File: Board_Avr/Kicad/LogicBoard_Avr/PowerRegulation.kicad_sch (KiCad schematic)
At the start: 8 parts, among them U3 LM1117-3.3, U4 LM1117-5.0

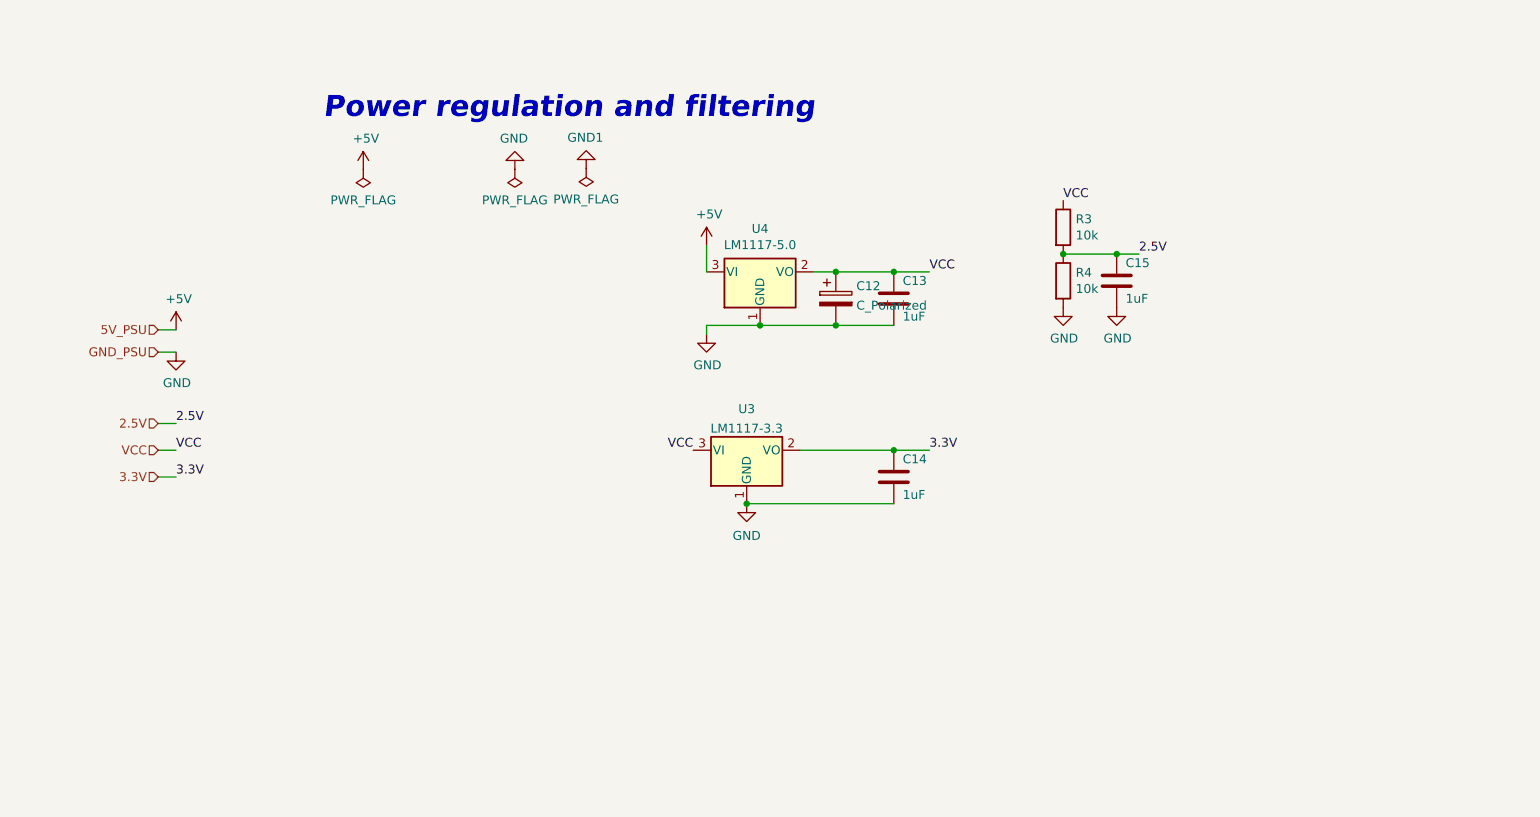
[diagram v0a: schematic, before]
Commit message: Added several external connections and reworked leds and output signals
Signed-off-by: bebenlebricolo <benoittarrade@hotmail.fr>
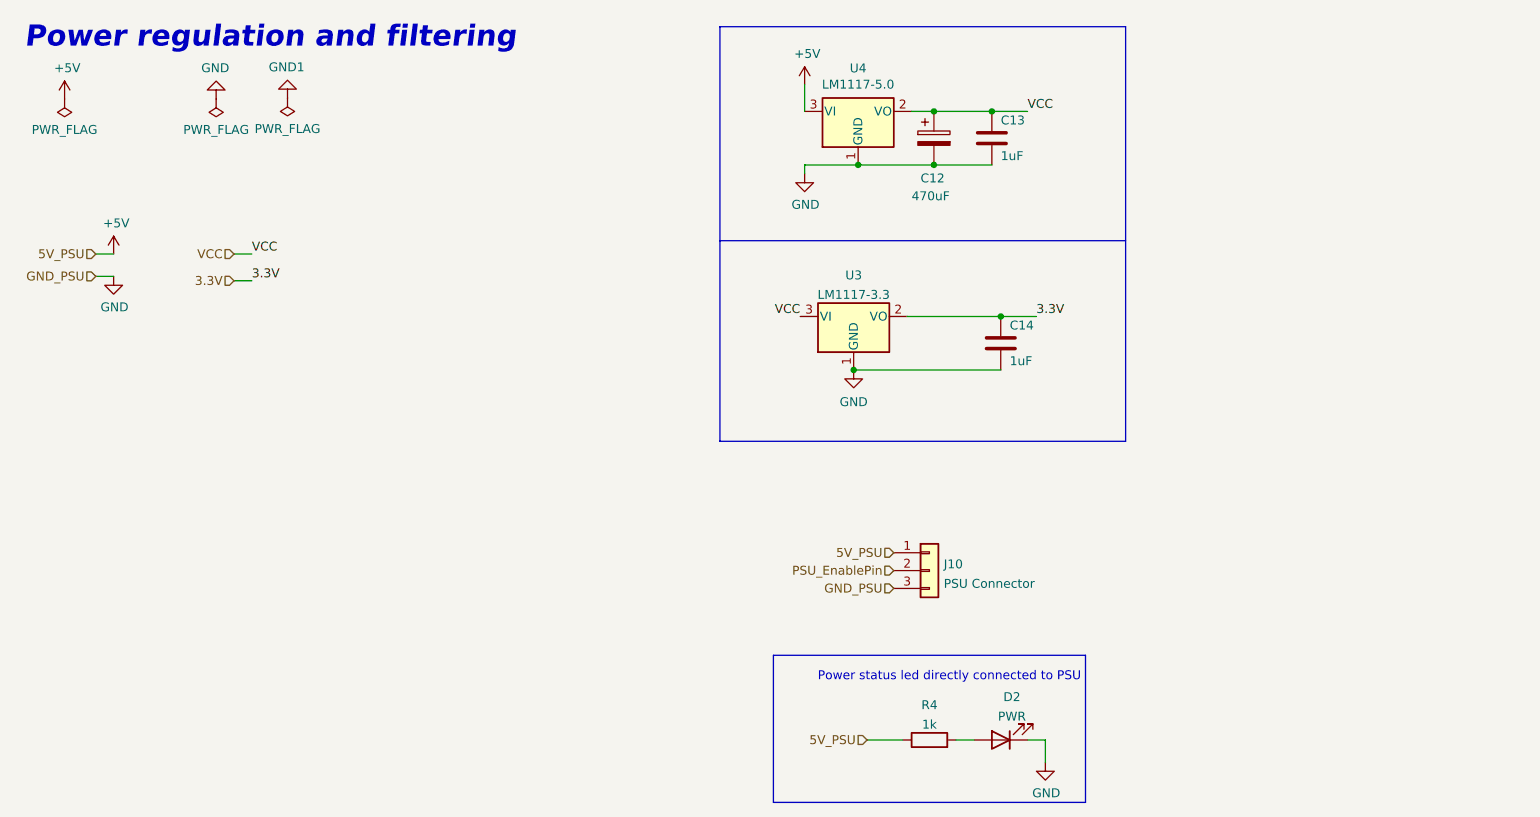
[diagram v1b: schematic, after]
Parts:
- removed C15: 1uF, Capacitor_SMD:C_1206_3216Metric_Pad1.33x1.80mm_HandSolder, symbol Device:C
- removed R3: 10k, Resistor_SMD:R_1206_3216Metric_Pad1.30x1.75mm_HandSolder, symbol Device:R
- added D2: PWR, symbol Device:LED
- added J10: PSU Connector, symbol Connector_Generic:Conn_01x03
- C12: value C_Polarized -> 470uF
- R4: value 10k -> 1k; footprint Resistor_SMD:R_1206_3216Metric_Pad1.30x1.75mm_HandSolder -> (none)
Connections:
- net 2.5V is gone; now on net +5V: R4.1
- net +5V: now also J10.1 (Pin_1)
- net GND: now also D2.1 (K), J10.3 (Pin_3); no longer R4.2
- new net: D2.2 (A), R4.2
- new net PSU_EnablePin: J10.2 (Pin_2)
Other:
- note added: "Power status led directly connected to PSU"
- moved on the sheet: C12, C13, C14, U3, U4

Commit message: Fixed misorganised pins and updated pin mapping table
Signed-off-by: bebenlebricolo <benoittarrade@hotmail.fr>
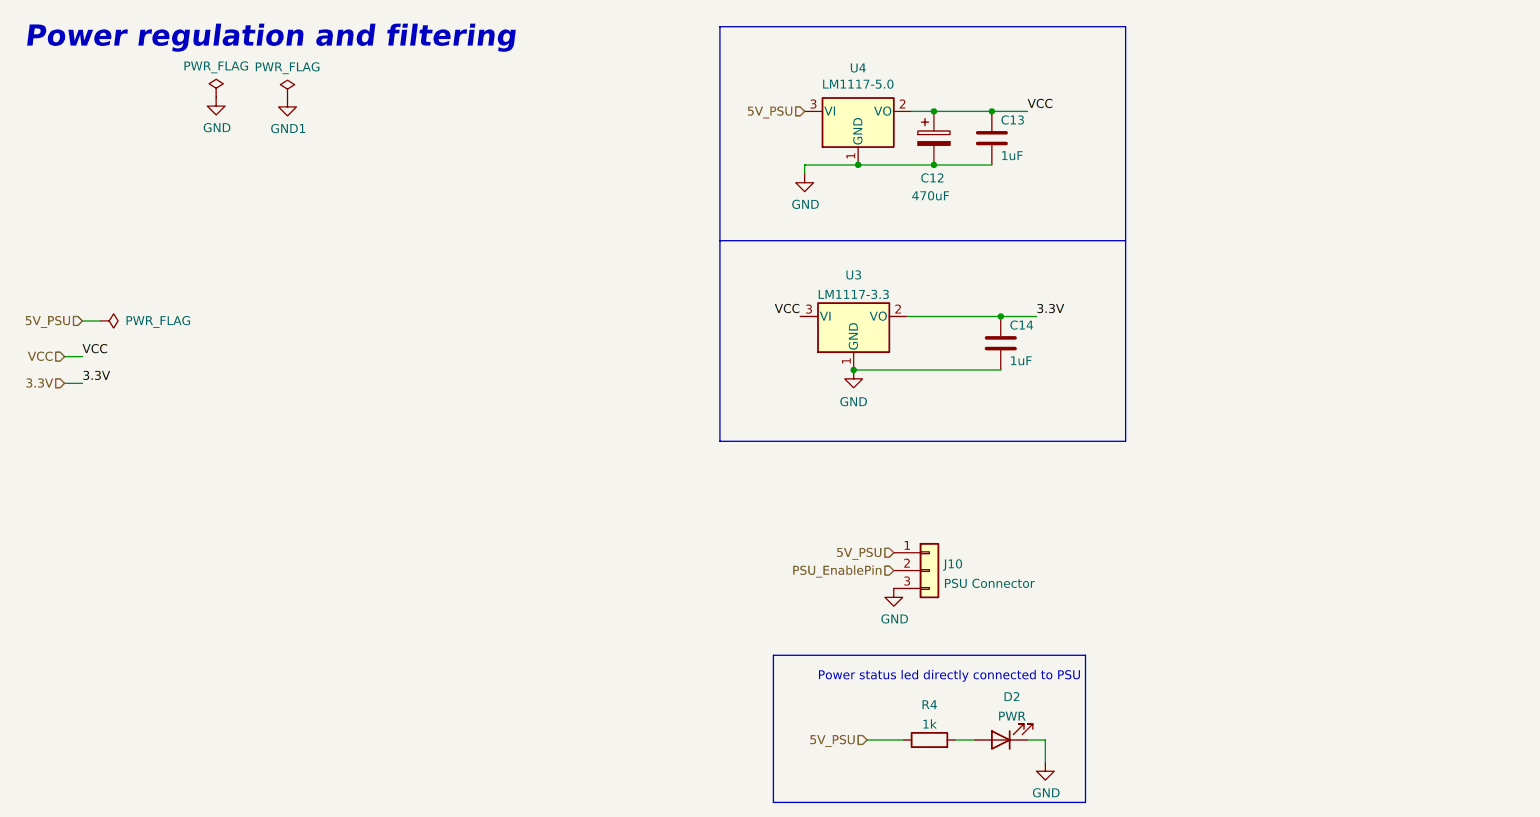
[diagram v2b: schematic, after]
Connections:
- net +5V renamed 5V_PSU
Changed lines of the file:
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@@
     (stroke (width 0) (type default) (color 0 0 0 0))
   )
-  (wire (pts (xy 59.055 53.975) (xy 61.595 53.975))
-    (stroke (width 0) (type default) (color 0 0 0 0))
-  )
-  (wire (pts (xy 39.37 53.975) (xy 41.91 53.975))
+  (wire (pts (xy 34.925 68.58) (xy 37.465 68.58))
+    (stroke (width 0) (type default) (color 0 0 0 0))
+  )
+  (wire (pts (xy 37.465 63.5) (xy 40.005 63.5))
     (stroke (width 0) (type default) (color 0 0 0 0))
   )
@@
     (stroke (width 0) (type default) (color 0 0 0 0))
   )
-  (wire (pts (xy 39.37 57.15) (xy 41.91 57.15))
-    (stroke (width 0) (type default) (color 0 0 0 0))
-  )
   (wire (pts (xy 161.925 123.19) (xy 164.465 123.19))
     (stroke (width 0) (type default) (color 0 0 0 0))
@@
     (stroke (width 0) (type default) (color 0 0 0 0))
   )
-  (wire (pts (xy 59.055 57.785) (xy 61.595 57.785))
-    (stroke (width 0) (type default) (color 0 0 0 0))
-  )
-  (wire (pts (xy 140.335 29.845) (xy 140.335 33.655))
+  (wire (pts (xy 34.925 72.39) (xy 37.465 72.39))
     (stroke (width 0) (type default) (color 0 0 0 0))
   )
@@
     (effects (font (size 1.27 1.27)) (justify left bottom))
   )
-  (label "3.3V" (at 61.595 57.785 0)
+  (label "3.3V" (at 37.465 72.39 0)
     (effects (font (size 1.27 1.27)) (justify left bottom))
   )
-  (label "VCC" (at 61.595 53.975 0)
+  (label "VCC" (at 37.465 68.58 0)
     (effects (font (size 1.27 1.27)) (justify left bottom))
   )
@@
     (effects (font (size 1.27 1.27)) (justify right))
   )
-  (hierarchical_label "3.3V" (shape input) (at 59.055 57.785 180)
+  (hierarchical_label "3.3V" (shape input) (at 34.925 72.39 180)
     (effects (font (size 1.27 1.27)) (justify right))
   )
@@
     (effects (font (size 1.27 1.27)) (justify right))
   )
-  (hierarchical_label "GND_PSU" (shape input) (at 39.37 57.15 180)
-    (effects (font (size 1.27 1.27)) (justify right))
-  )
-  (hierarchical_label "GND_PSU" (shape input) (at 153.035 101.6 180)
-    (effects (font (size 1.27 1.27)) (justify right))
-  )
-  (hierarchical_label "VCC" (shape input) (at 59.055 53.975 180)
-    (effects (font (size 1.27 1.27)) (justify right))
-  )
-  (hierarchical_label "5V_PSU" (shape input) (at 39.37 53.975 180)
+  (hierarchical_label "5V_PSU" (shape input) (at 140.335 33.655 180)
+    (effects (font (size 1.27 1.27)) (justify right))
+  )
+  (hierarchical_label "VCC" (shape input) (at 34.925 68.58 180)
+    (effects (font (size 1.27 1.27)) (justify right))
+  )
+  (hierarchical_label "5V_PSU" (shape input) (at 37.465 63.5 180)
     (effects (font (size 1.27 1.27)) (justify right))
   )
@@
     (effects (font (size 1.27 1.27)) (justify right))
   )
-  (symbol (lib_id "power:GND1") (at 66.675 31.75 180) (unit 1)
-    (in_bom yes) (on_board yes)
-    (property "Reference" "#PWR0125" (id 0) (at 66.675 25.4 0)
-      (effects (font (size 1.27 1.27)) hide)
-    )
-    (property "Value" "GND1" (id 1) (at 66.548 27.3558 0))
+  (symbol (lib_id "power:GND1") (at 66.675 31.75 0) (unit 1)
+    (in_bom yes) (on_board yes)
+    (property "Reference" "#PWR0125" (id 0) (at 66.675 38.1 0)
+      (effects (font (size 1.27 1.27)) hide)
+    )
+    (property "Value" "GND1" (id 1) (at 66.802 36.1442 0))
     (property "Footprint" "" (id 2) (at 66.675 31.75 0)
       (effects (font (size 1.27 1.27)) hide)
@@
     (pin "3")
   )
-  (symbol (lib_id "power:GND") (at 41.91 57.15 0) (unit 1)
-    (in_bom yes) (on_board yes)
-    (property "Reference" "#PWR0123" (id 0) (at 41.91 63.5 0)
-      (effects (font (size 1.27 1.27)) hide)
-    )
-    (property "Value" "GND" (id 1) (at 42.037 61.5442 0))
-    (property "Footprint" "" (id 2) (at 41.91 57.15 0)
-      (effects (font (size 1.27 1.27)) hide)
-    )
-    (property "Datasheet" "" (id 3) (at 41.91 57.15 0)
-      (effects (font (size 1.27 1.27)) hide)
-    )
-    (pin "1")
-  )
   (symbol (lib_id "Device:C") (at 167.005 37.465 0) (unit 1)
     (in_bom yes) (on_board yes)
@@
     (pin "2")
   )
-  (symbol (lib_id "power:PWR_FLAG") (at 66.675 31.75 180) (unit 1)
-    (in_bom yes) (on_board yes)
-    (property "Reference" "#FLG0101" (id 0) (at 66.675 33.655 0)
-      (effects (font (size 1.27 1.27)) hide)
-    )
-    (property "Value" "PWR_FLAG" (id 1) (at 66.675 36.1442 0))
+  (symbol (lib_id "power:PWR_FLAG") (at 66.675 31.75 0) (unit 1)
+    (in_bom yes) (on_board yes)
+    (property "Reference" "#FLG0101" (id 0) (at 66.675 29.845 0)
+      (effects (font (size 1.27 1.27)) hide)
+    )
+    (property "Value" "PWR_FLAG" (id 1) (at 66.675 27.3558 0))
     (property "Footprint" "" (id 2) (at 66.675 31.75 0)
       (effects (font (size 1.27 1.27)) hide)
@@
     (pin "1")
   )
-  (symbol (lib_id "power:GND") (at 56.515 31.877 180) (unit 1)
-    (in_bom yes) (on_board yes)
-    (property "Reference" "#PWR0128" (id 0) (at 56.515 25.527 0)
-      (effects (font (size 1.27 1.27)) hide)
-    )
-    (property "Value" "GND" (id 1) (at 56.388 27.4828 0))
-    (property "Footprint" "" (id 2) (at 56.515 31.877 0)
-      (effects (font (size 1.27 1.27)) hide)
-    )
-    (property "Datasheet" "" (id 3) (at 56.515 31.877 0)
-      (effects (font (size 1.27 1.27)) hide)
-    )
-    (pin "1")
-  )
-  (symbol (lib_id "power:+5V") (at 34.925 31.877 0) (unit 1)
-    (in_bom yes) (on_board yes)
-    (property "Reference" "#PWR0127" (id 0) (at 34.925 35.687 0)
-      (effects (font (size 1.27 1.27)) hide)
-    )
-    (property "Value" "+5V" (id 1) (at 35.306 27.4828 0))
-    (property "Footprint" "" (id 2) (at 34.925 31.877 0)
-      (effects (font (size 1.27 1.27)) hide)
-    )
-    (property "Datasheet" "" (id 3) (at 34.925 31.877 0)
+  (symbol (lib_id "power:GND") (at 153.035 101.6 0) (unit 1)
+    (in_bom yes) (on_board yes)
+    (property "Reference" "#PWR0120" (id 0) (at 153.035 107.95 0)
+      (effects (font (size 1.27 1.27)) hide)
+    )
+    (property "Value" "GND" (id 1) (at 153.162 105.9942 0))
+    (property "Footprint" "" (id 2) (at 153.035 101.6 0)
+      (effects (font (size 1.27 1.27)) hide)
+    )
+    (property "Datasheet" "" (id 3) (at 153.035 101.6 0)
+      (effects (font (size 1.27 1.27)) hide)
+    )
+    (pin "1")
+  )
+  (symbol (lib_id "power:GND") (at 56.515 31.623 0) (unit 1)
+    (in_bom yes) (on_board yes)
+    (property "Reference" "#PWR0128" (id 0) (at 56.515 37.973 0)
+      (effects (font (size 1.27 1.27)) hide)
+    )
+    (property "Value" "GND" (id 1) (at 56.642 36.0172 0))
+    (property "Footprint" "" (id 2) (at 56.515 31.623 0)
+      (effects (font (size 1.27 1.27)) hide)
+    )
+    (property "Datasheet" "" (id 3) (at 56.515 31.623 0)
       (effects (font (size 1.27 1.27)) hide)
     )
@@
     (pin "1")
     (pin "2")
-  )
-  (symbol (lib_id "power:+5V") (at 41.91 53.975 0) (unit 1)
-    (in_bom yes) (on_board yes)
-    (property "Reference" "#PWR0122" (id 0) (at 41.91 57.785 0)
-      (effects (font (size 1.27 1.27)) hide)
-    )
-    (property "Value" "+5V" (id 1) (at 42.291 49.5808 0))
-    (property "Footprint" "" (id 2) (at 41.91 53.975 0)
-      (effects (font (size 1.27 1.27)) hide)
-    )
-    (property "Datasheet" "" (id 3) (at 41.91 53.975 0)
-      (effects (font (size 1.27 1.27)) hide)
-    )
-    (pin "1")
   )
   (symbol (lib_id "power:GND") (at 174.625 126.365 0) (unit 1)
@@
     (pin "1")
   )
-  (symbol (lib_id "power:PWR_FLAG") (at 56.515 31.877 180) (unit 1)
-    (in_bom yes) (on_board yes)
-    (property "Reference" "#FLG0102" (id 0) (at 56.515 33.782 0)
-      (effects (font (size 1.27 1.27)) hide)
-    )
-    (property "Value" "PWR_FLAG" (id 1) (at 56.515 36.2712 0))
-    (property "Footprint" "" (id 2) (at 56.515 31.877 0)
-      (effects (font (size 1.27 1.27)) hide)
-    )
-    (property "Datasheet" "~" (id 3) (at 56.515 31.877 0)
-      (effects (font (size 1.27 1.27)) hide)
-    )
-    (pin "1")
-  )
-  (symbol (lib_id "power:+5V") (at 140.335 29.845 0) (unit 1)
-    (in_bom yes) (on_board yes)
-    (property "Reference" "#PWR0126" (id 0) (at 140.335 33.655 0)
-      (effects (font (size 1.27 1.27)) hide)
-    )
-    (property "Value" "+5V" (id 1) (at 140.716 25.4508 0))
-    (property "Footprint" "" (id 2) (at 140.335 29.845 0)
-      (effects (font (size 1.27 1.27)) hide)
-    )
-    (property "Datasheet" "" (id 3) (at 140.335 29.845 0)
-      (effects (font (size 1.27 1.27)) hide)
-    )
-    (pin "1")
-  )
-  (symbol (lib_id "power:PWR_FLAG") (at 34.925 31.877 180) (unit 1)
-    (in_bom yes) (on_board yes)
-    (property "Reference" "#FLG0103" (id 0) (at 34.925 33.782 0)
-      (effects (font (size 1.27 1.27)) hide)
-    )
-    (property "Value" "PWR_FLAG" (id 1) (at 34.925 36.2712 0))
-    (property "Footprint" "" (id 2) (at 34.925 31.877 0)
-      (effects (font (size 1.27 1.27)) hide)
-    )
-    (property "Datasheet" "~" (id 3) (at 34.925 31.877 0)
-      (effects (font (size 1.27 1.27)) hide)
-    )
+  (symbol (lib_id "power:PWR_FLAG") (at 56.515 31.623 0) (unit 1)
+    (in_bom yes) (on_board yes)
+    (property "Reference" "#FLG0102" (id 0) (at 56.515 29.718 0)
+      (effects (font (size 1.27 1.27)) hide)
+    )
+    (property "Value" "PWR_FLAG" (id 1) (at 56.515 27.2288 0))
+    (property "Footprint" "" (id 2) (at 56.515 31.623 0)
+      (effects (font (size 1.27 1.27)) hide)
+    )
+    (property "Datasheet" "~" (id 3) (at 56.515 31.623 0)
+      (effects (font (size 1.27 1.27)) hide)
+    )
+    (pin "1")
+  )
+  (symbol (lib_id "power:PWR_FLAG") (at 40.005 63.5 270) (unit 1)
+    (in_bom yes) (on_board yes)
+    (property "Reference" "#FLG0103" (id 0) (at 41.91 63.5 0)
+      (effects (font (size 1.27 1.27)) hide)
+    )
+    (property "Value" "PWR_FLAG" (id 1) (at 48.26 63.5 90))
+    (property "Footprint" "" (id 2) (at 40.005 63.5 0)
+      (effects (font (size 1.27 1.27)) hide)
+    )
+    (property "Datasheet" "~" (id 3) (at 40.005 63.5 0)
+      (effects (font (size 1.27 1.27)) hide)
+    )
